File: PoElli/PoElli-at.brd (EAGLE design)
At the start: 100 x 80 mm, 121 parts, among them J1 DF12-ELLI-HEADER-TOP, Q1 FDV301N, Q2 SI1307DL, T1 Coilcraft 230NL, U1 FST3257, U3 NCP1117, X1 POE-TP-RJ45-MOLEX, Y1 25MHz

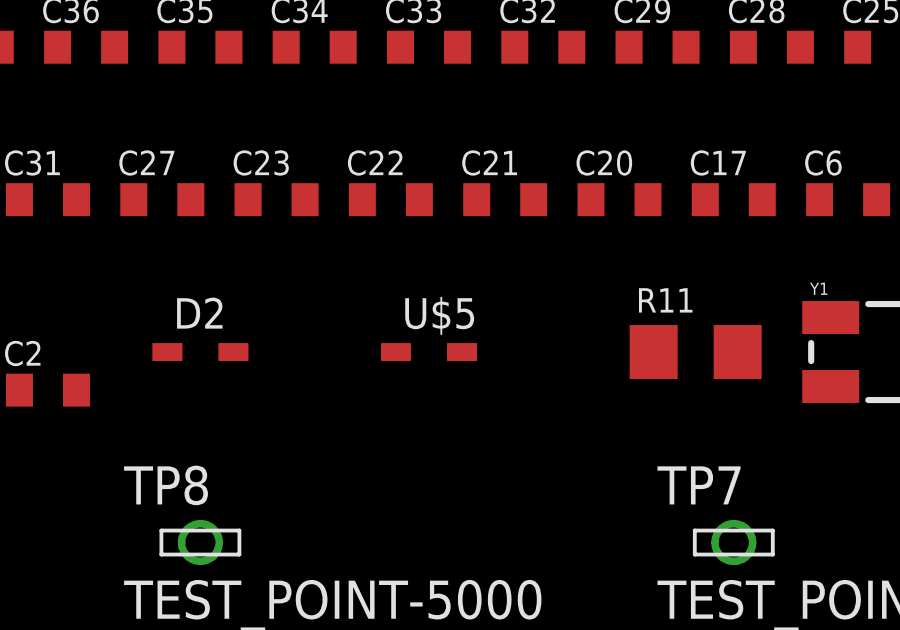
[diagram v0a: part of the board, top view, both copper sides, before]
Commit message: Move BAV20WS to Ell-i-DiscreteSemi.lbr
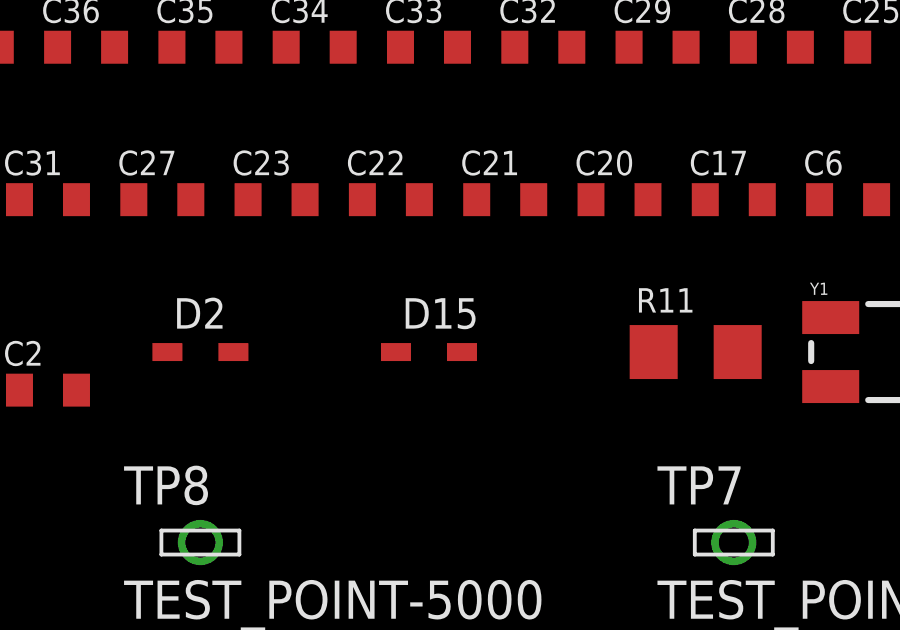
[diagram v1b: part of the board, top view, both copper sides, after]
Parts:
- removed U$5: BAV20WS, TPS2378:SOD323
- added D15: BAV20WS, ELL-i-DIscreteSemi:SOD323
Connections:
- net N$28: now also D15.1; no longer U$5.1
- net N$33: now also D15.2; no longer U$5.2
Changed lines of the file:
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@@
 <element name="C8" library="ELL-i-Passives" package="C0805" value="4u7" x="60.96" y="63.5"/>
 <element name="R13" library="ELL-i-Passives" package="R0402" value="6k04" x="49.53" y="76.2"/>
-<element name="U$5" library="TPS2378" package="SOD323" value="BAV20WS" x="38.1" y="53.34"/>
+<element name="D15" library="ELL-i-DIscreteSemi" package="SOD323" value="BAV20WS" x="38.1" y="53.34"/>
 <element name="R14" library="ELL-i-Passives" package="R0805" value="2k" x="95.25" y="68.58"/>
 <element name="C9" library="ELL-i-Passives" package="C0805" value="100nF" x="95.25" y="58.42"/>
@@
 <contactref element="U$3" pad="F1"/>
 <contactref element="R12" pad="1"/>
-<contactref element="U$5" pad="1"/>
+<contactref element="D15" pad="1"/>
 <contactref element="U$7" pad="5"/>
 <wire x1="37" y1="53.34" x2="4.52" y2="16.39" width="0" layer="19" extent="1-1"/>
@@
 <signal name="N$33">
 <contactref element="C9" pad="2"/>
-<contactref element="U$5" pad="2"/>
+<contactref element="D15" pad="2"/>
 <contactref element="R14" pad="1"/>
 <wire x1="96.2" y1="58.42" x2="94.3" y2="68.58" width="0" layer="19" extent="1-1"/>

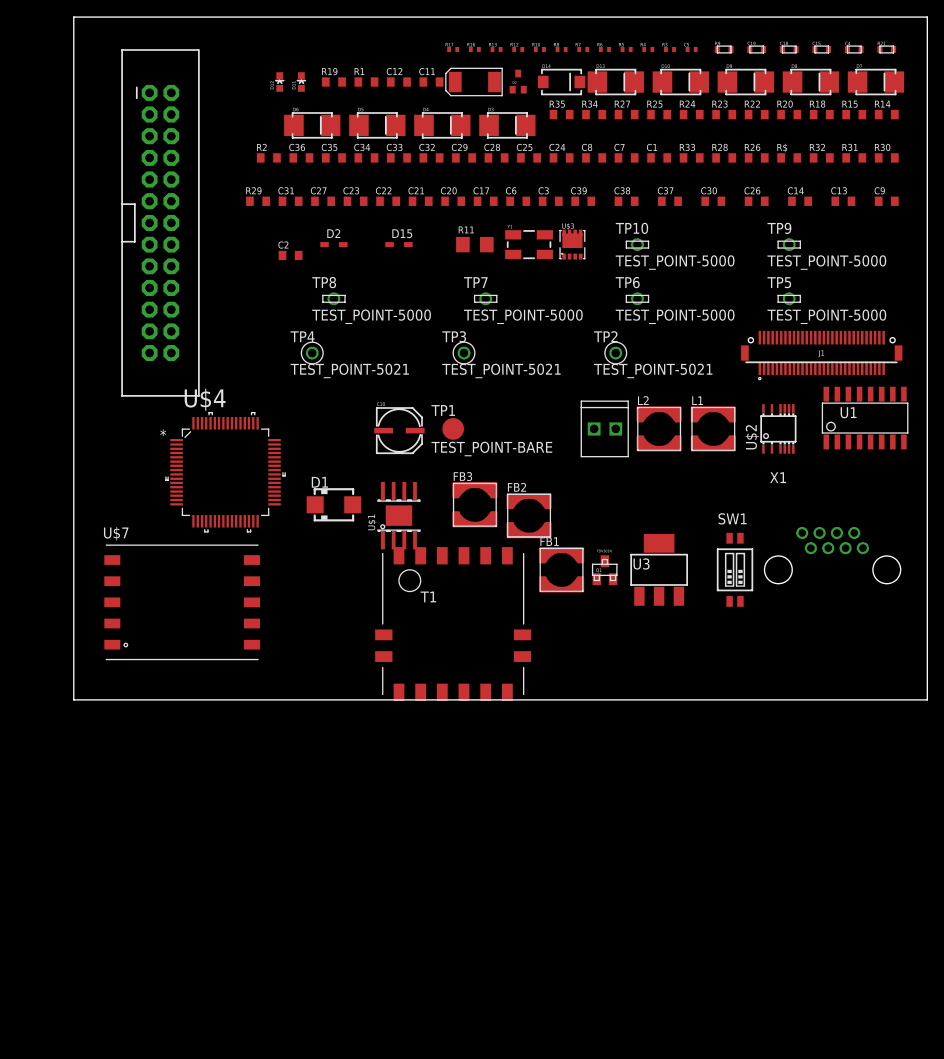
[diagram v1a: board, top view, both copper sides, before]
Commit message: Manually renamed PoElli components other than R,C,D
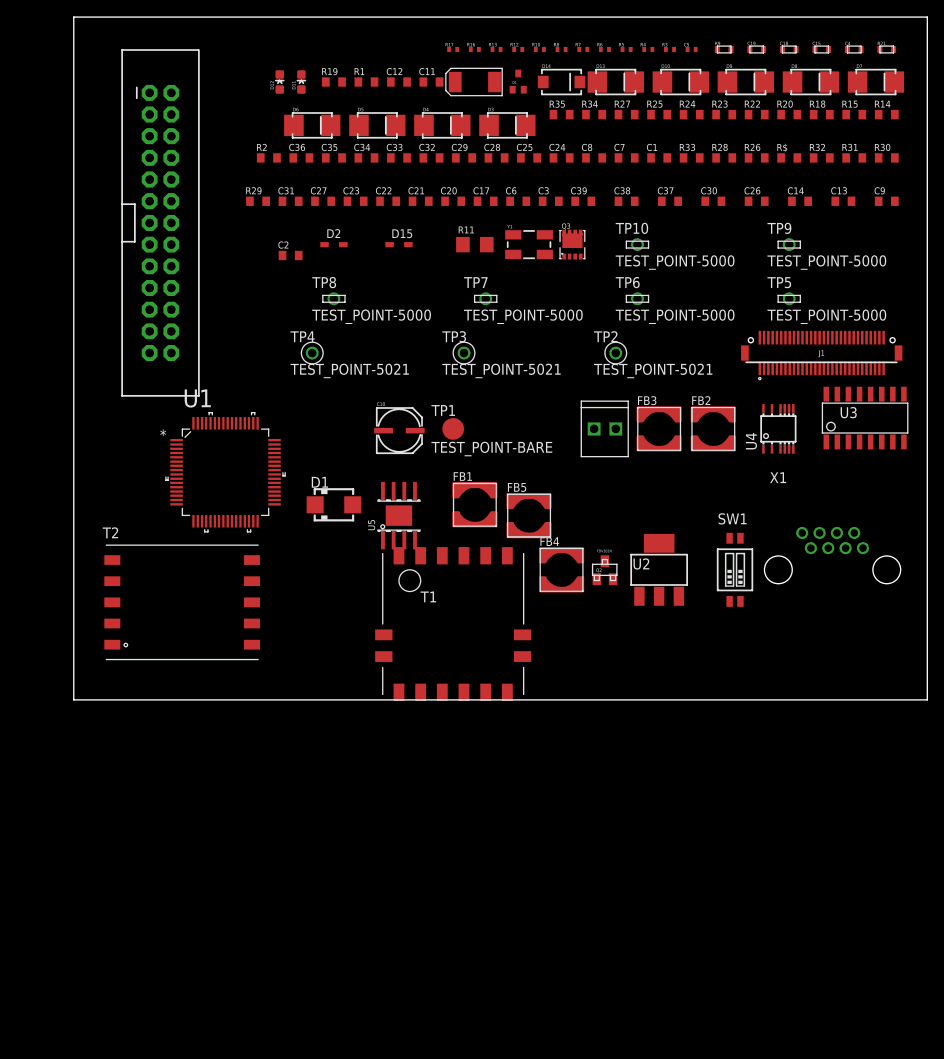
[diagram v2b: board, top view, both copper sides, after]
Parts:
- removed L1, L2: (no value), ELL-i-Passives:COILCRAFT-MSS5121
- removed U$4: ENC624J600-I/PT, ELL-i-DigitalIC:QFP50P1200X1200X120-64N
- added FB4, FB5: 2A, ELL-i-Passives:COILCRAFT-MSS5121
- added U2: NCP1117, ell-i:SOT223
- D15: device ELL-i-DIscreteSemi:SOD323 -> ELL-i-DIscreteSemi:SOD-323
- FB1: value 2A -> LQM15
- FB2: value 2A -> (none)
- FB3: value LQM15 -> (none)
- Q1: value FDV301N -> SI1307DL; device ELL-i-DIscreteSemi:SOT-23 -> ELL-i-DIscreteSemi:SOT-323
- Q2: value SI1307DL -> FDV301N; device ELL-i-DIscreteSemi:SOT-323 -> ELL-i-DIscreteSemi:SOT-23
- U1: value FST3257 -> ENC624J600-I/PT; device ELL-i-DigitalIC:SOIC-16-NARROW -> ELL-i-DigitalIC:QFP50P1200X1200X120-64N
- U3: value NCP1117 -> FST3257; device ell-i:SOT223 -> ELL-i-DigitalIC:SOIC-16-NARROW
- moved U1 75.2 mm to (17.8, 26.7)
- moved Q1 58.0 mm to (52.1, 72.4)
- moved Q2 58.0 mm to (62.2, 15.2)
- moved U3 30.0 mm to (92.7, 33.0)
- moved FB2 23.9 mm to (74.9, 31.8)
- moved FB3 23.3 mm to (68.6, 31.8)
- moved FB1 12.7 mm to (47.0, 22.9)
- renumbered U$1 to U5, U$2 to U4, U$3 to Q3, U$7 to T2
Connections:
- net +3V3: now also Q1.P$2, U2.2, U2.4; no longer Q2.P$2, U3.2, U3.4
- net 5V: now also U2.3; no longer U3.3
- net ENC-3V3: now also FB1.2, U1.21, U1.22, U1.25, U1.28, U1.4, U1.47, U1.64; no longer FB3.2, U$4.21, U$4.22, U$4.25, U$4.28, U$4.4, U$4.47, U$4.64
- net ETH_INT: now also U1.34; no longer U$4.34
- net ETH_MISO: now also U1.50; no longer U$4.50
- net ETH_MOSI: now also U1.51; no longer U$4.51
- net ETH_MUX: now also Q2.P$1, U3.1; no longer Q1.P$1, U1.1
- net ETH_SCK: now also U1.52; no longer U$4.52
- net GND: now also FB5.2; no longer FB2.2
- net GNDA: now also Q2.P$2, U1.1, U1.10, U1.11, U1.12, U1.13, U1.17, U1.18, U1.19, U1.20, U1.23, U1.24, U1.29, U1.32, U1.35, U1.36, U1.37, U1.38, U1.39, U1.40, U1.41, U1.42, U1.43, U1.44, U1.45, U1.46, U1.48, U1.5, U1.53, U1.54, U1.55, U1.56, U1.57, U1.58, U1.59, U1.6, U1.60, U1.61, U1.62, U1.7, U1.9, U3.15, U3.8; no longer Q1.P$2, U$4.1, U$4.10, U$4.11, U$4.12, U$4.13, U$4.17, U$4.18, U$4.19, U$4.20, U$4.23, U$4.24, U$4.29, U$4.32, U$4.35, U$4.36, U$4.37, U$4.38, U$4.39, U$4.40, U$4.41, U$4.42, U$4.43, U$4.44, U$4.45, U$4.46, U$4.48, U$4.5, U$4.53, U$4.54, U$4.55, U$4.56, U$4.57, U$4.58, U$4.59, U$4.6, U$4.60, U$4.61, U$4.62, U$4.7, U$4.8, U$4.9, U1.15
- net N$11: now also U3.12; no longer U1.12
- net N$12: now also U3.9; no longer U1.9
- net N$13: now also U3.7; no longer U1.7
- net N$14: now also U3.4; no longer U1.4
- net N$15: now also FB3.2; no longer L2.2
- net N$16: now also FB2.2; no longer L1.2
- net N$35: now also U1.49; no longer U$4.49
- net N$37: now also U1.2; no longer U$4.2
- net N$39: now also U1.27; no longer U$4.27
- net N$41: now also U1.14; no longer U$4.14
- net N$42: now also U1.15; no longer U$4.15
- net N$43: now also U3.16; no longer U1.16
- net N$45: now also U1.16; no longer U$4.16
- net N$46: now also U1.63; no longer U$4.63
- net N$47: now also U1.3; no longer U$4.3
- net N$53: now also FB4.1; no longer FB1.1
- net N$55: now also FB5.1; no longer FB2.1
- net N$56: now also Q2.P$3; no longer Q1.P$3
- net N$57: now also Q1.P$1; no longer Q2.P$1
- net N$58: now also U2.1; no longer U3.1
- net N$59: now also U1.26; no longer U$4.26
- net N$6: now also FB2.1; no longer L1.1
- net N$60: now also FB1.1, Q1.P$3; no longer FB3.1, Q2.P$3
- net N$61: now also U3.3; no longer U1.3
- net N$62: now also U1.30, U3.13; no longer U$4.30, U1.13
- net N$63: now also U1.31, U3.10; no longer U$4.31, U1.10
- net N$64: now also U3.6; no longer U1.6
- net N$76: now also FB4.2; no longer FB1.2
- net N$8: now also FB3.1; no longer L2.1
- net RX+: now also U3.5; no longer U1.5
- net RX-: now also U3.2; no longer U1.2
- net TX+: now also U3.14; no longer U1.14
- net TX-: now also U3.11; no longer U1.11

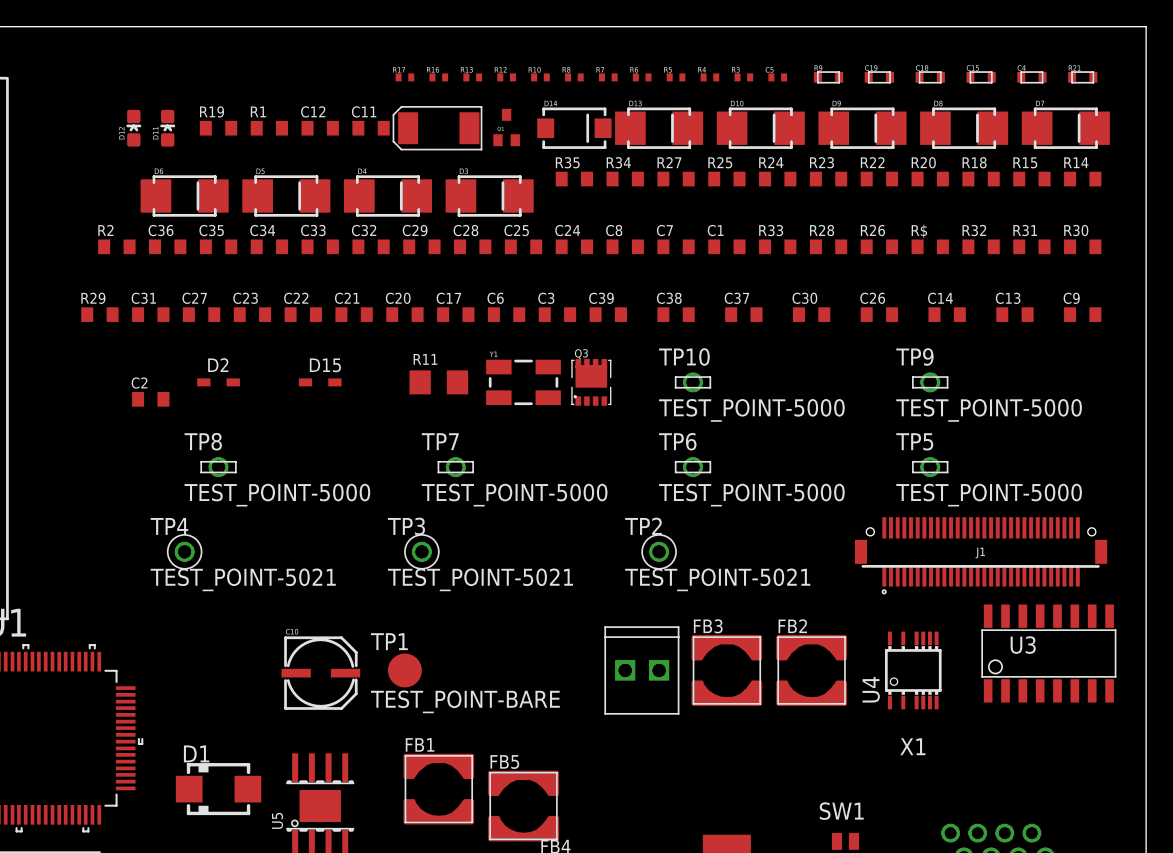
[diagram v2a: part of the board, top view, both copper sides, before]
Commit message: Renamed R,C,D in PoElli
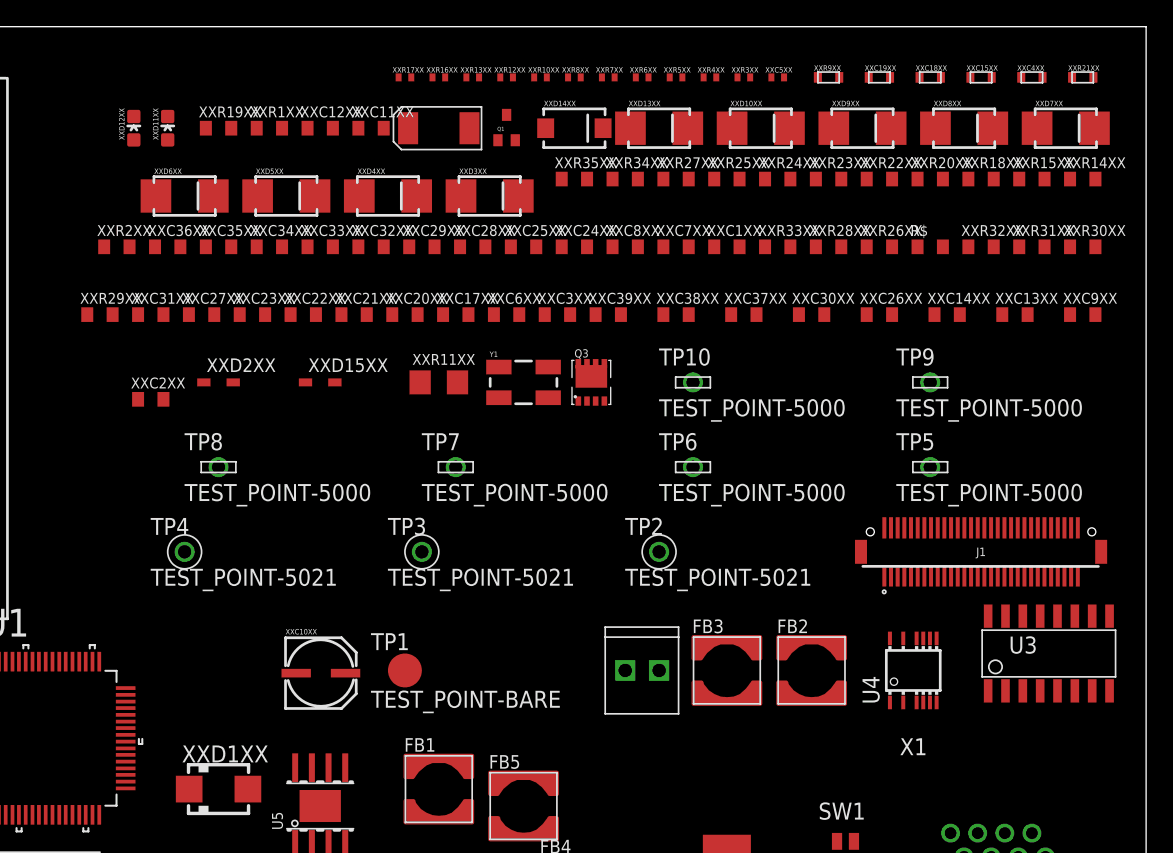
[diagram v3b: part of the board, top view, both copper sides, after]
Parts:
- renumbered C1 to XXC1XX, C10 to XXC10XX, C11 to XXC11XX, C12 to XXC12XX, C13 to XXC13XX, C14 to XXC14XX, C15 to XXC15XX, C16 to XXC16XX, C17 to XXC17XX, C18 to XXC18XX, C19 to XXC19XX, C2 to XXC2XX, C20 to XXC20XX, C21 to XXC21XX, C22 to XXC22XX, C23 to XXC23XX, C24 to XXC24XX, C25 to XXC25XX, C26 to XXC26XX, C27 to XXC27XX, C28 to XXC28XX, C29 to XXC29XX, C3 to XXC3XX, C30 to XXC30XX, C31 to XXC31XX, C32 to XXC32XX, C33 to XXC33XX, C34 to XXC34XX, C35 to XXC35XX, C36 to XXC36XX, C37 to XXC37XX, C38 to XXC38XX, C39 to XXC39XX, C4 to XXC4XX, C5 to XXC5XX, C6 to XXC6XX, C7 to XXC7XX, C8 to XXC8XX, C9 to XXC9XX, D1 to XXD1XX, D10 to XXD10XX, D11 to XXD11XX, D12 to XXD12XX, D13 to XXD13XX, D14 to XXD14XX, D15 to XXD15XX, D2 to XXD2XX, D3 to XXD3XX, D4 to XXD4XX, D5 to XXD5XX, D6 to XXD6XX, D7 to XXD7XX, D8 to XXD8XX, D9 to XXD9XX, R1 to XXR1XX, R10 to XXR10XX, R11 to XXR11XX, R12 to XXR12XX, R13 to XXR13XX, R14 to XXR14XX, R15 to XXR15XX, R16 to XXR16XX, R17 to XXR17XX, R18 to XXR18XX, R19 to XXR19XX, R2 to XXR2XX, R20 to XXR20XX, R21 to XXR21XX, R22 to XXR22XX, R23 to XXR23XX, R24 to XXR24XX, R25 to XXR25XX, R26 to XXR26XX, R27 to XXR27XX, R28 to XXR28XX, R29 to XXR29XX, R3 to XXR3XX, R30 to XXR30XX, R31 to XXR31XX, R32 to XXR32XX, R33 to XXR33XX, R34 to XXR34XX, R35 to XXR35XX, R4 to XXR4XX, R5 to XXR5XX, R6 to XXR6XX, R7 to XXR7XX, R8 to XXR8XX, R9 to XXR9XX

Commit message: Fix previous commit screwups + cleanups to PoElli
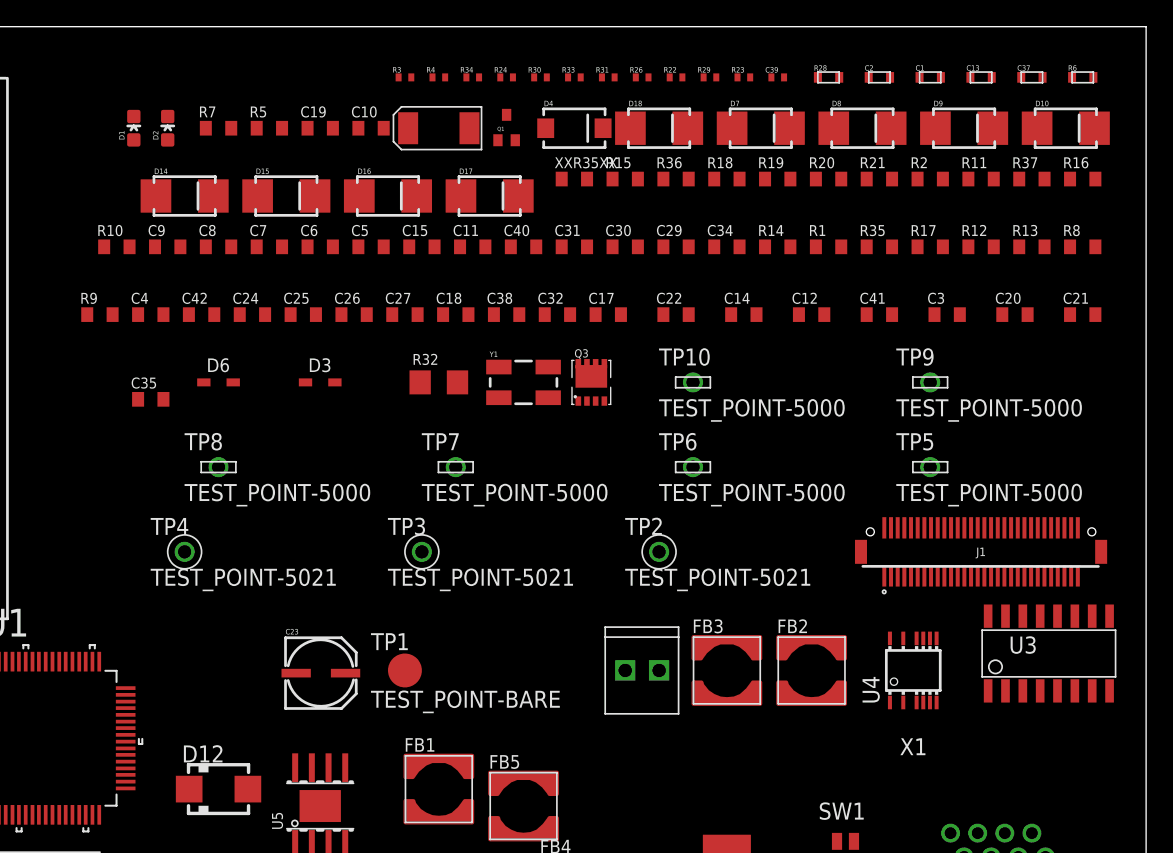
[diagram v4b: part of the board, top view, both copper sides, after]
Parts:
- C10, C19: value (none) -> 10nF
- R5: value (none) -> 10R
- R7: value (none) -> 10K
- renumbered R$ to R17, XXC10XX to C23, XXC11XX to C10, XXC12XX to C19, XXC13XX to C20, XXC14XX to C3, XXC15XX to C13, XXC16XX to C16, XXC17XX to C18, XXC18XX to C1, XXC19XX to C2, XXC1XX to C34, XXC20XX to C27, XXC21XX to C26, XXC22XX to C25, XXC23XX to C24, XXC24XX to C31, XXC25XX to C40, XXC26XX to C41, XXC27XX to C42, XXC28XX to C11, XXC29XX to C15, XXC2XX to C35, XXC30XX to C12, XXC31XX to C4, XXC32XX to C5, XXC33XX to C6, XXC34XX to C7, XXC35XX to C8, XXC36XX to C9, XXC37XX to C14, XXC38XX to C22, XXC39XX to C17, XXC3XX to C32, XXC4XX to C37, XXC5XX to C39, XXC6XX to C38, XXC7XX to C29, XXC8XX to C30, XXC9XX to C21, XXD10XX to D7, XXD11XX to D2, XXD12XX to D1, XXD13XX to D18, XXD14XX to D4, XXD15XX to D3, XXD1XX to D12, XXD2XX to D6, XXD3XX to D17, XXD4XX to D16, XXD5XX to D15, XXD6XX to D14, XXD7XX to D10, XXD8XX to D9, XXD9XX to D8, XXR10XX to R30, XXR11XX to R32, XXR12XX to R24, XXR13XX to R34, XXR14XX to R16, XXR15XX to R37, XXR16XX to R4, XXR17XX to R3, XXR18XX to R11, XXR19XX to R7, XXR1XX to R5, XXR20XX to R2, XXR21XX to R6, XXR22XX to R21, XXR23XX to R20, XXR24XX to R19, XXR25XX to R18, XXR26XX to R35, XXR27XX to R36, XXR28XX to R1, XXR29XX to R9, XXR2XX to R10, XXR30XX to R8, XXR31XX to R13, XXR32XX to R12, XXR33XX to R14, XXR34XX to R15, XXR3XX to R23, XXR4XX to R29, XXR5XX to R22, XXR6XX to R26, XXR7XX to R31, XXR8XX to R33, XXR9XX to R28
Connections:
- net N$10 renamed POE_A+
- net N$5 renamed POE_B-
- net N$61 renamed TPIN-
- net N$64 renamed TPIN+
- net N$7 renamed POE_B+
- net N$9 renamed POE_A-
- removed net N$62: R13.1, U1.30, U3.13
- removed net N$63: R12.1, U1.31, U3.10
- new net TPOUT+: R12.1, U1.31, U3.13
- new net TPOUT-: R13.1, U1.30, U3.10
- net N$40: now also T1.3

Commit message: Cleanups to PoElli schematics
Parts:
- FB2, FB3: value (none) -> 2A
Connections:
- net GND renamed RTN
- net N$15 renamed VSS
- net N$16 renamed VDD
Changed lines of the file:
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@@
 </element>
 <element name="C34" library="ELL-i-Passives" package="C0805" value="1nF" x="68.58" y="63.5"/>
-<element name="FB2" library="ELL-i-Passives" package="COILCRAFT-MSS5121" value="" x="74.93" y="31.75"/>
-<element name="FB3" library="ELL-i-Passives" package="COILCRAFT-MSS5121" value="" x="68.58" y="31.75"/>
+<element name="FB2" library="ELL-i-Passives" package="COILCRAFT-MSS5121" value="2A" x="74.93" y="31.75"/>
+<element name="FB3" library="ELL-i-Passives" package="COILCRAFT-MSS5121" value="2A" x="68.58" y="31.75"/>
 <element name="D12" library="ell-i" package="SMA" value="SMAJ58A" x="30.48" y="22.86"/>
 <element name="C35" library="ELL-i-Passives" package="C0805" value="100nF" x="25.4" y="52.07"/>
@@
 <wire x1="66.58" y1="29.75" x2="69.53" y2="63.5" width="0" layer="19" extent="1-1"/>
 </signal>
-<signal name="N$15">
+<signal name="VSS">
 <contactref element="FB3" pad="2"/>
 <contactref element="D12" pad="2"/>
@@
 </signal>
 <signal name="N$17">
-<contactref element="R22" pad="1"/>
 <contactref element="R26" pad="2"/>
 <contactref element="U4" pad="3"/>
+<contactref element="R22" pad="1"/>
 <wire x1="62.705" y1="76.2" x2="64.295" y2="76.2" width="0" layer="19" extent="1-1"/>
 <wire x1="81.8" y1="29.35" x2="64.295" y2="76.2" width="0" layer="19" extent="1-1"/>
 </signal>
-<signal name="GND">
+<signal name="RTN">
 <contactref element="R26" pad="1"/>
 <contactref element="C32" pad="2"/>
@@
 <wire x1="51.34" y1="19.59" x2="63.5" y2="31.75" width="0" layer="19" extent="1-1"/>
 </signal>
-<signal name="N$16">
+<signal name="VDD">
 <contactref element="D18" pad="C"/>
 <contactref element="D12" pad="1"/>

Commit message: Further cleanups and add components to PoElli schematics
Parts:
- added C28: 33nF, ELL-i-Passives:C0805
- added C33: 150pF NP, ELL-i-Passives:C0805
- added D11: BAS70J, ELL-i-DIscreteSemi:SOD323
- added D13: TBD 18V, SparkFun-DiscreteSemi:SMB-DIODE
- added J3: M022.54MM_SCREWTERM, SparkFun-Connectors:1X02_2.54_SCREWTERM
- added R25: 100K, ELL-i-Passives:R0603
- added R27: 220R, ELL-i-Passives:R1206
- added R38: 0R, ELL-i-Passives:R0603
- C38: value 470p -> 6n8; device ELL-i-Passives:C0805 -> ELL-i-Passives:C0402
- C39: value 6n8 -> 470p; device ELL-i-Passives:C0402 -> ELL-i-Passives:C0805
- D6: device TPS2378:SOD323 -> ELL-i-DIscreteSemi:SOD323
- moved C38 27.0 mm to (72.4, 76.2)
- moved C39 27.0 mm to (52.1, 58.4)
- renumbered JP1 to J4
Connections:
- net N$34 renamed UNREG_5V+
- removed net N$58: C16.P$2, C17.2, C18.2, C23.-, T2.10, T2.9, TP4.P$1, U2.1
- new net GND: C28.1, R27.2
- new net N$10: J3.P2
- new net N$15: C33.2, R27.1
- new net N$9: D11.2, D13.C, R25.2, R38.2, U5.7
- net GNDA: now also C16.P$2, C17.2, C18.2, C23.-, C28.2, T2.10, T2.9, TP4.P$1, U2.1
- net N$17: now also D11.1
- net N$20: now also R38.1; no longer U5.7
- net N$22: now also C39.1; no longer C38.1
- net N$23: now also C38.1; no longer C39.1
- net N$28: now also C33.1
- net RTN: now also D13.A
- net VDD: now also J3.P1, R25.1

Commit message: Small cleanups to PoElli
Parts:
- R38: value 0R -> 0R NP
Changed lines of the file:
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@@
 <element name="XXR35XX" library="ELL-i-Passives" package="R0805" value="47k" x="57.15" y="68.58"/>
 <element name="SW1" library="SparkFun-Electromechanical" package="DIPSWITCH-02-50MIL" value="" x="77.47" y="15.24"/>
-<element name="R38" library="ELL-i-Passives" package="R0603" value="0R" x="2.54" y="-2.54"/>
+<element name="R38" library="ELL-i-Passives" package="R0603" value="0R NP" x="2.54" y="-2.54"/>
 <element name="R25" library="ELL-i-Passives" package="R0603" value="100K" x="2.54" y="-5.08"/>
 <element name="D11" library="ELL-i-DIscreteSemi" package="SOD323" value="BAS70J" x="2.54" y="-8.89"/>
